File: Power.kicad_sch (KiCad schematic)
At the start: 61 parts, among them U10 TPS63002, U2 TPS63001, U8 TPS63002

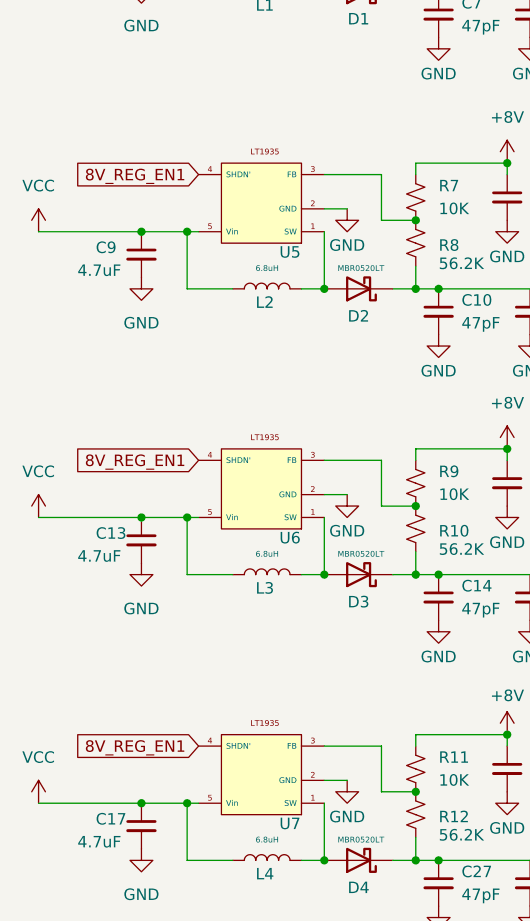
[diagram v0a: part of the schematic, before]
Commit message: General Layout Complete
Completed general layout, beginning to add debugging components such as test points and
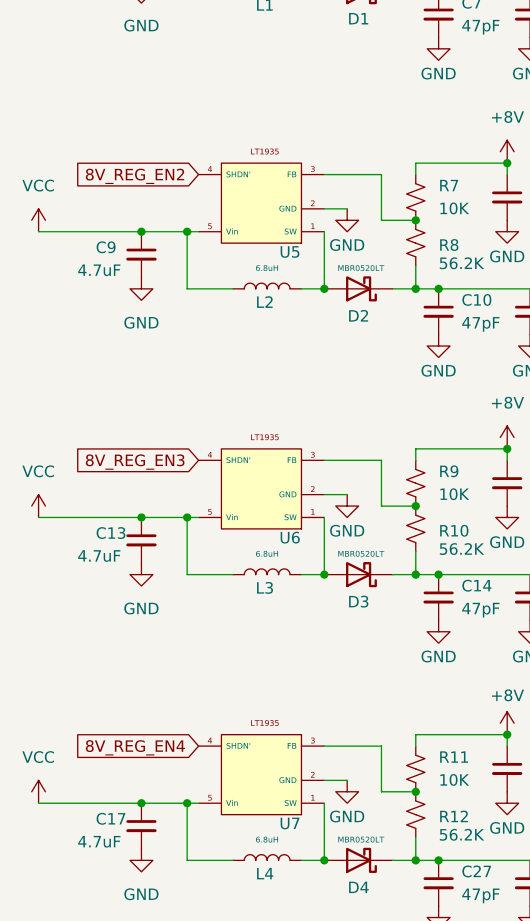
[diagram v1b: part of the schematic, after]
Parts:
- U4, U5, U6, U7: value ~ -> (none)
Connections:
- net 8V_REG_EN1: no longer U5.4 (SHDN'), U6.4 (SHDN'), U7.4 (SHDN')
- new net 8V_REG_EN2: U5.4 (SHDN')
- new net 8V_REG_EN3: U6.4 (SHDN')
- new net 8V_REG_EN4: U7.4 (SHDN')

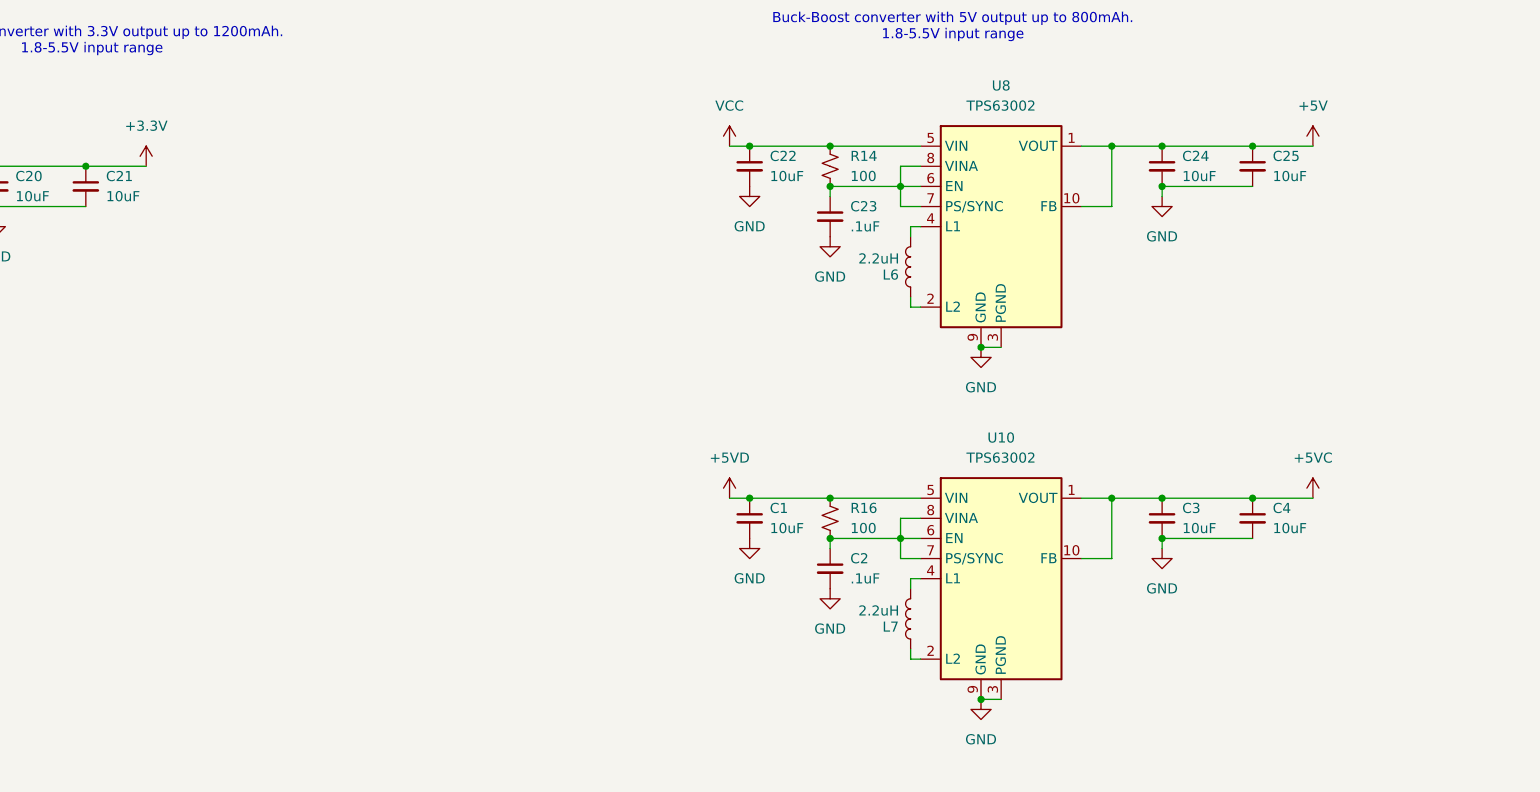
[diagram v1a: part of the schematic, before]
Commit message: testpoints on board
Organized testpoints on board. Still need to fix bus for general purpose GPIO and route traces for LEDs.
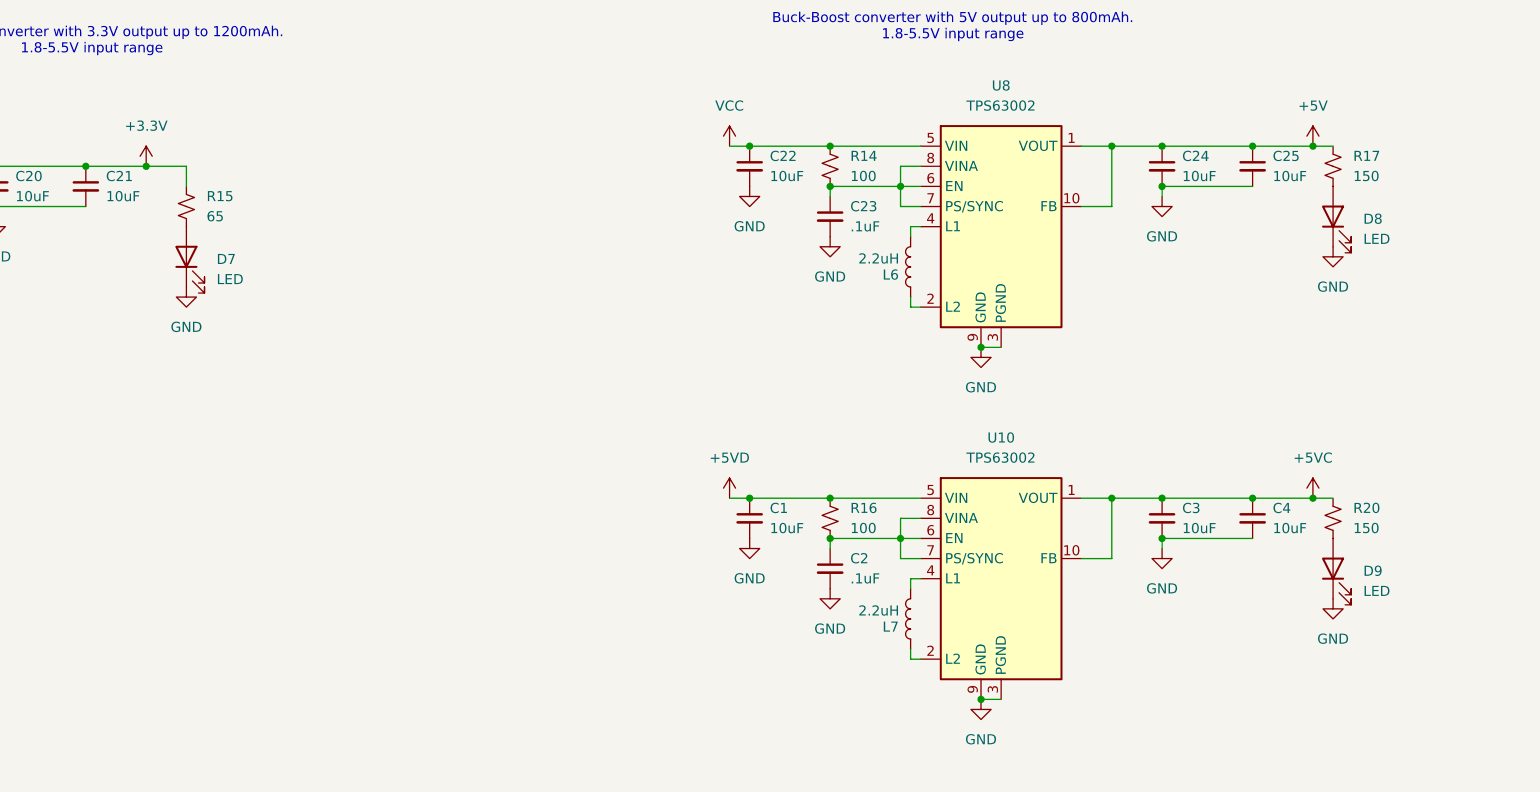
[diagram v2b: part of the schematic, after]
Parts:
- added D7, D8, D9: LED, Capacitor_SMD:C_0603_1608Metric_Pad1.08x0.95mm_HandSolder, symbol Device:LED
- added R15: 65, Resistor_SMD:R_0805_2012Metric_Pad1.20x1.40mm_HandSolder, symbol Device:R_Small_US
- added R17, R20: 150, Resistor_SMD:R_0805_2012Metric_Pad1.20x1.40mm_HandSolder, symbol Device:R_Small_US
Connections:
- net +3.3V: now also R15.1
- net +5V: now also R17.1
- net +5VC: now also R20.1
- net GND: now also D7.1 (K), D8.1 (K), D9.1 (K)
- new net: D8.2 (A), R17.2
- new net: D9.2 (A), R20.2
- new net: D7.2 (A), R15.2
